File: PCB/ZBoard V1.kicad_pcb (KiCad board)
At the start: 2 copper layers, 143 parts, among them SW1 SW_Push, SW10 SW_Push, SW11 SW_Push, SW12 SW_Push, SW13 SW_Push, SW14 SW_Push, SW15 SW_Push, SW16 SW_Push, SW17 SW_Push, SW18 SW_Push, SW19 SW_Push, SW2 SW_Push, SW20 SW_Push, SW21 SW_Push, SW22 SW_Push, SW23 SW_Push, SW24 SW_Push, SW25 SW_Push, SW26 SW_Push, SW27 SW_Push, SW28 SW_Push, SW29 SW_Push, SW3 SW_Push, SW30 SW_Push, SW31 SW_Push, SW32 SW_Push, SW33 SW_Push, SW34 SW_Push, SW35 SW_Push, SW36 SW_Push, SW37 SW_Push, SW38 SW_Push, SW39 SW_Push, SW4 SW_Push, SW40 SW_Push, SW41 SW_Push, SW42 SW_Push, SW43 SW_Push, SW44 SW_Push, SW45 SW_Push, SW46 SW_Push, SW47 SW_Push, SW48 SW_Push, SW49 SW_Push, SW5 SW_Push, SW50 SW_Push, SW51 SW_Push, SW52 SW_Push, SW53 SW_Push, SW54 SW_Push, SW55 SW_Push, SW56 SW_Push, SW57 SW_Push, SW58 SW_Push, SW59 SW_Push, SW6 SW_Push, SW60 SW_Push, SW7 SW_Push, SW8 SW_Push, SW9 SW_Push, U1 XIAO-nRF52840-SMD, U2 XIAO-nRF52840-SMD

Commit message: Finish PCB routing
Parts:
- removed 2M1, 2M2, 806k1, 806k2: R, Diode_SMD:D_SOD-123
- removed BO1, BO2, BO3: break off, Mousebites:mouse-bite-5mm-slot
- removed H1, H10, H2, H3, H4, H5, H6, H7, H8, H9: MountingHole, Mousebites:mouse-bite-5mm-slot
- removed TP3, TP4: GND, TestPoint:TestPoint_Pad_D2.0mm
- added D61: D, Diode_SMD:D_SOD-123, F.Cu at (204.8, 23.8)
- added D62: D, Diode_SMD:D_SOD-123, F.Cu at (204.8, 42.9)
- added D63: D, Diode_SMD:D_SOD-123, F.Cu at (214.3, 61.9)
- added D64: D, Diode_SMD:D_SOD-123, F.Cu at (219.1, 81.0)
- added D65: D, Diode_SMD:D_SOD-123, F.Cu at (228.6, 100.0)
- added D66: D, Diode_SMD:D_SOD-123, F.Cu at (223.8, 23.8)
- added D67: D, Diode_SMD:D_SOD-123, F.Cu at (223.8, 42.9)
- added D68: D, Diode_SMD:D_SOD-123, F.Cu at (233.4, 61.9)
- added D69: D, Diode_SMD:D_SOD-123, F.Cu at (238.1, 81.0)
- added D70: D, Diode_SMD:D_SOD-123, F.Cu at (247.7, 100.0)
- added D71: D, Diode_SMD:D_SOD-123, F.Cu at (242.9, 23.8)
- added D72: D, Diode_SMD:D_SOD-123, F.Cu at (242.9, 42.9)
- added D73: D, Diode_SMD:D_SOD-123, F.Cu at (252.4, 61.9)
- added D74: D, Diode_SMD:D_SOD-123, F.Cu at (257.2, 81.0)
- added D75: D, Diode_SMD:D_SOD-123, F.Cu at (281.0, 100.0)
- added D76: D, Diode_SMD:D_SOD-123, F.Cu at (261.9, 23.8)
- added D77: D, Diode_SMD:D_SOD-123, F.Cu at (261.9, 42.9)
- added D78: D, Diode_SMD:D_SOD-123, F.Cu at (271.5, 61.9)
- added D79: D, Diode_SMD:D_SOD-123, F.Cu at (300.0, 81.0)
- added D80: D, Diode_SMD:D_SOD-123, F.Cu at (300.0, 100.0)
- added D81: D, Diode_SMD:D_SOD-123, F.Cu at (281.0, 23.8)
- added D82: D, Diode_SMD:D_SOD-123, F.Cu at (300.0, 42.9)
- added D83: D, Diode_SMD:D_SOD-123, F.Cu at (300.0, 61.9)
- added D84: D, Diode_SMD:D_SOD-123, F.Cu at (300.0, 23.8)
- added R1: 806k, MFR-25FRF52-806k:MFR-25FRF52-806k, F.Cu at (340.5, 54.8)
- added R2: 2M, MFR-25FRF52-2M:MFR-25FRF52-2M, F.Cu at (340.5, 69.1)
- added SW61: SW_Push, Gateron_KS33_Hotswap:Gateron-KS33-Hotswap-1U, F.Cu at (214.3, 23.8)
- added SW62: SW_Push, Gateron_KS33_Hotswap:Gateron-KS33-Hotswap-1U, F.Cu at (214.3, 42.9)
- added SW63: SW_Push, Gateron_KS33_Hotswap:Gateron-KS33-Hotswap-1U, F.Cu at (223.8, 61.9)
- added SW64: SW_Push, Gateron_KS33_Hotswap:Gateron-KS33-Hotswap-1U, F.Cu at (228.6, 81.0)
- added SW65: SW_Push, Gateron_KS33_Hotswap:Gateron-KS33-Hotswap-1U, F.Cu at (238.1, 100.0)
- added SW66: SW_Push, Gateron_KS33_Hotswap:Gateron-KS33-Hotswap-1U, F.Cu at (233.4, 23.8)
- added SW67: SW_Push, Gateron_KS33_Hotswap:Gateron-KS33-Hotswap-1U, F.Cu at (233.4, 42.9)
- added SW68: SW_Push, Gateron_KS33_Hotswap:Gateron-KS33-Hotswap-1U, F.Cu at (242.9, 61.9)
- added SW69: SW_Push, Gateron_KS33_Hotswap:Gateron-KS33-Hotswap-1U, F.Cu at (247.7, 81.0)
- added SW70: SW_Push, Gateron_KS33_Hotswap:Gateron-KS33-Hotswap-1.75U, F.Cu at (264.3, 100.0)
- added SW71: SW_Push, Gateron_KS33_Hotswap:Gateron-KS33-Hotswap-1U, F.Cu at (252.4, 23.8)
- added SW72: SW_Push, Gateron_KS33_Hotswap:Gateron-KS33-Hotswap-1U, F.Cu at (252.4, 42.9)
- added SW73: SW_Push, Gateron_KS33_Hotswap:Gateron-KS33-Hotswap-1U, F.Cu at (261.9, 61.9)
- added SW74: SW_Push, Gateron_KS33_Hotswap:Gateron-KS33-Hotswap-2.25U, F.Cu at (278.6, 81.0)
- added SW75: SW_Push, Gateron_KS33_Hotswap:Gateron-KS33-Hotswap-1U, F.Cu at (290.5, 100.0)
- added SW76: SW_Push, Gateron_KS33_Hotswap:Gateron-KS33-Hotswap-1U, F.Cu at (271.5, 23.8)
- added SW77: SW_Push, Gateron_KS33_Hotswap:Gateron-KS33-Hotswap-2U, F.Cu at (281.0, 42.9)
- added SW78: SW_Push, Gateron_KS33_Hotswap:Gateron-KS33-Hotswap-1.5U, F.Cu at (285.8, 61.9)
- added SW79: SW_Push, Gateron_KS33_Hotswap:Gateron-KS33-Hotswap-1U, F.Cu at (309.6, 81.0)
- added SW80: SW_Push, Gateron_KS33_Hotswap:Gateron-KS33-Hotswap-1U, F.Cu at (309.6, 100.0)
- added SW81: SW_Push, Gateron_KS33_Hotswap:Gateron-KS33-Hotswap-1U, F.Cu at (290.5, 23.8)
- added SW82: SW_Push, Gateron_KS33_Hotswap:Gateron-KS33-Hotswap-1U, F.Cu at (309.6, 42.9)
- added SW83: SW_Push, Gateron_KS33_Hotswap:Gateron-KS33-Hotswap-1U, F.Cu at (309.6, 61.9)
- added SW84: SW_Push, Gateron_KS33_Hotswap:Gateron-KS33-Hotswap-1U, F.Cu at (309.6, 23.8)
- SW1, SW10, SW11, SW13, SW14, SW15, SW16, SW17, SW19, SW2, SW20, SW21, SW22, SW23, SW25, SW26, SW27, SW28, SW29, SW30, SW31, SW32, SW33, SW34, SW35, SW36, SW37, SW38, SW39, SW40, SW41, SW42, SW43, SW44, SW45, SW46, SW47, SW48, SW49, SW50, SW51, SW52, SW53, SW54, SW55, SW56, SW57, SW58, SW59, SW60, SW7, SW8, SW9: footprint PCM_marbastlib-xp-gateron_lp:SW_KS33_HS_KS-2P02B01-02_HS_1u -> Gateron_KS33_Hotswap:Gateron-KS33-Hotswap-1U
- SW12, SW18, SW6: footprint PCM_marbastlib-xp-gateron_lp:SW_KS33_HS_KS-2P02B01-02_HS_1u -> Gateron_KS33_Hotswap:Gateron-KS33-Hotswap-1.25U
- SW24: footprint PCM_marbastlib-xp-gateron_lp:SW_KS33_HS_KS-2P02B01-02_HS_1u -> Gateron_KS33_Hotswap:Gateron-KS33-Hotswap-6.25U
- SW3: footprint PCM_marbastlib-xp-gateron_lp:SW_KS33_HS_KS-2P02B01-02_HS_1u -> Gateron_KS33_Hotswap:Gateron-KS33-Hotswap-1.5U
- SW4: footprint PCM_marbastlib-xp-gateron_lp:SW_KS33_HS_KS-2P02B01-02_HS_1u -> Gateron_KS33_Hotswap:Gateron-KS33-Hotswap-1.75U
- SW5: footprint PCM_marbastlib-xp-gateron_lp:SW_KS33_HS_KS-2P02B01-02_HS_1u -> Gateron_KS33_Hotswap:Gateron-KS33-Hotswap-2.25U
- TP2: value BAT -> GND; footprint TestPoint:TestPoint_Pad_D2.0mm -> TestPoint:TestPoint_Pad_2.0x2.0mm
- U2: value XIAO-nRF52840-SMD -> MCP23017-E_SP; footprint Modified-XIAO:modified-XIAO-nRF52840-SMD -> MCP23017_GPIO:MCP23107_GPIO
- moved TP2 306.1 mm to (340.5, 45.2)
- moved U2 281.1 mm to (330.2, 57.8)
- moved D60 255.1 mm to (300.0, 119.1), turned to -90 degrees
- moved D54 235.8 mm to (281.0, 119.1), turned to -90 degrees
- moved D48 223.6 mm to (261.9, 119.1), turned to -90 degrees
- moved D1 208.0 mm to (14.3, 23.8), turned to -90 degrees
- moved D42 203.8 mm to (242.9, 119.1), turned to -90 degrees
- moved SW60 201.6 mm to (309.6, 119.1)
- moved D7 200.2 mm to (33.3, 23.8), turned to -90 degrees
- moved D13 194.5 mm to (52.4, 23.8), turned to -90 degrees
- moved SW54 191.7 mm to (290.5, 119.1)
- moved TP1 190.4 mm to (340.5, 40.5)
- moved D3 188.6 mm to (14.3, 61.9), turned to -90 degrees
- moved D36 184.4 mm to (223.8, 119.1), turned to -90 degrees
- moved SW48 182.6 mm to (271.5, 119.1)
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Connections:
- net /left/VBAT renamed /VBAT
- D1 pad 1: /left/ROW0 -> /ROW1
- D10 pad 1: /right/ROW0 -> /ROW4
- D11 pad 1: /left/ROW0 -> /ROW5
- D12 pad 1: /right/ROW0 -> /ROW6
- D13 pad 1: /left/ROW1 -> /ROW1
- D14 pad 1: /right/ROW1 -> /ROW2
- D15 pad 1: /left/ROW1 -> /ROW3
- D16 pad 1: /right/ROW1 -> /ROW4
- D17 pad 1: /left/ROW1 -> /ROW5
- D18 pad 1: /right/ROW1 -> /ROW6
- D19 pad 1: /left/ROW1 -> /ROW1
- D2 pad 1: /right/ROW0 -> /ROW2
- D20 pad 1: /right/ROW1 -> /ROW2
- D21 pad 1: /left/ROW1 -> /ROW3
- D22 pad 1: /right/ROW1 -> /ROW4
- D23 pad 1: /left/ROW1 -> /ROW5
- D24 pad 1: /right/ROW1 -> /ROW6
- D25 pad 1: /left/ROW2 -> /ROW1
- D26 pad 1: /right/ROW2 -> /ROW2
- D27 pad 1: /left/ROW2 -> /ROW3
- D28 pad 1: /right/ROW2 -> /ROW4
- D29 pad 1: /left/ROW2 -> /ROW5
- D3 pad 1: /left/ROW0 -> /ROW3
- D30 pad 1: /right/ROW2 -> /ROW6
- D31 pad 1: /left/ROW2 -> /ROW1
- D32 pad 1: /right/ROW2 -> /ROW2
- D33 pad 1: /left/ROW2 -> /ROW3
- D34 pad 1: /right/ROW2 -> /ROW4
- D35 pad 1: /left/ROW2 -> /ROW5
- D36 pad 1: /right/ROW2 -> /ROW6
- D37 pad 1: /left/ROW3 -> /ROW1
- D38 pad 1: /right/ROW3 -> /ROW2
- D39 pad 1: /left/ROW3 -> /ROW3
- D4 pad 1: /right/ROW0 -> /ROW4
- D40 pad 1: /right/ROW3 -> /ROW4
- D41 pad 1: /left/ROW3 -> /ROW5
- D42 pad 1: /right/ROW3 -> /ROW6
- D43 pad 1: /left/ROW3 -> /ROW1
- D44 pad 1: /right/ROW3 -> /ROW2
- D45 pad 1: /left/ROW3 -> /ROW3
- D46 pad 1: /right/ROW3 -> /ROW4
- D47 pad 1: /left/ROW3 -> /ROW5
- D48 pad 1: /right/ROW3 -> /ROW6
- D49 pad 1: /left/ROW4 -> /ROW1
- D5 pad 1: /left/ROW0 -> /ROW5
- D50 pad 1: /right/ROW4 -> /ROW2
- D51 pad 1: /left/ROW4 -> /ROW3
- D52 pad 1: /right/ROW4 -> /ROW4
- D53 pad 1: /left/ROW4 -> /ROW5
- D54 pad 1: /right/ROW4 -> /ROW6
- D55 pad 1: /left/ROW4 -> /ROW1
- D56 pad 1: /right/ROW4 -> /ROW2
- D57 pad 1: /left/ROW4 -> /ROW3
- D58 pad 1: /right/ROW4 -> /ROW4
- D59 pad 1: /left/ROW4 -> /ROW5
- D6 pad 1: /right/ROW0 -> /ROW6
- D60 pad 1: /right/ROW4 -> /ROW6
- D7 pad 1: /left/ROW0 -> /ROW1
- D8 pad 1: /right/ROW0 -> /ROW2
- D9 pad 1: /left/ROW0 -> /ROW3
- SW1 pad 1: /left/COL0 -> /COL1
- SW10 pad 1: /right/COL4 -> /COL2
- SW11 pad 1: /left/COL5 -> /COL2
- SW12 pad 1: /right/COL5 -> /COL2
- SW13 pad 1: /left/COL0 -> /COL3
- SW14 pad 1: /right/COL0 -> /COL3
- SW15 pad 1: /left/COL1 -> /COL3
- SW16 pad 1: /right/COL1 -> /COL3
- SW17 pad 1: /left/COL2 -> /COL3
- SW18 pad 1: /right/COL2 -> /COL3
- SW19 pad 1: /left/COL3 -> /COL4
- SW2 pad 1: /right/COL0 -> /COL1
- SW20 pad 1: /right/COL3 -> /COL4
- SW21 pad 1: /left/COL4 -> /COL4
- SW22 pad 1: /right/COL4 -> /COL4
- SW23 pad 1: /left/COL5 -> /COL4
- SW24 pad 1: /right/COL5 -> /COL4
- SW25 pad 1: /left/COL0 -> /COL5
- SW26 pad 1: /right/COL0 -> /COL5
- SW27 pad 1: /left/COL1 -> /COL5
- SW28 pad 1: /right/COL1 -> /COL5
- SW29 pad 1: /left/COL2 -> /COL5
- SW3 pad 1: /left/COL1 -> /COL1
- SW30 pad 1: /right/COL2 -> /COL5
- SW31 pad 1: /left/COL3 -> /COL6
- SW32 pad 1: /right/COL3 -> /COL6
- SW33 pad 1: /left/COL4 -> /COL6
- SW34 pad 1: /right/COL4 -> /COL6
- SW35 pad 1: /left/COL5 -> /COL6
- SW36 pad 1: /right/COL5 -> /COL6
- SW37 pad 1: /left/COL0 -> /COL7
- SW38 pad 1: /right/COL0 -> /COL7
- SW39 pad 1: /left/COL1 -> /COL7
- SW4 pad 1: /right/COL1 -> /COL1
- SW40 pad 1: /right/COL1 -> /COL7
- SW41 pad 1: /left/COL2 -> /COL7
- SW42 pad 1: /right/COL2 -> /COL7
- SW43 pad 1: /left/COL3 -> /COL8
- SW44 pad 1: /right/COL3 -> /COL8
- SW45 pad 1: /left/COL4 -> /COL8
- SW46 pad 1: /right/COL4 -> /COL8
- SW47 pad 1: /left/COL5 -> /COL8
- SW48 pad 1: /right/COL5 -> /COL8
- SW49 pad 1: /left/COL0 -> /COL9
- SW5 pad 1: /left/COL2 -> /COL1
- SW50 pad 1: /right/COL0 -> /COL9
- SW51 pad 1: /left/COL1 -> /COL9
- SW52 pad 1: /right/COL1 -> /COL9
- SW53 pad 1: /left/COL2 -> /COL9
- SW54 pad 1: /right/COL2 -> /COL9
- SW55 pad 1: /left/COL3 -> /COL10
- SW56 pad 1: /right/COL3 -> /COL10
- SW57 pad 1: /left/COL4 -> /COL10
- SW58 pad 1: /right/COL4 -> /COL10
- SW59 pad 1: /left/COL5 -> /COL10
- SW6 pad 1: /right/COL2 -> /COL1
- SW60 pad 1: /right/COL5 -> /COL10
- SW7 pad 1: /left/COL3 -> /COL2
- SW8 pad 1: /right/COL3 -> /COL2
- SW9 pad 1: /left/COL4 -> /COL2
- TP2 pad 1: /right/VBAT -> GND
- U1 pad 1: /left/BT_PIN -> /COL15
- U1 pad 10: /left/ROW2 -> /ROW4
- U1 pad 11: /left/ROW1 -> /ROW3
- U1 pad 14: unconnected-(U1-5V-Pad14) -> +5V
- U1 pad 2: /left/COL1 -> /COL16
- U1 pad 20: /left/COL0 -> unconnected-(U1-PA30_SWCLK-Pad20)
- U1 pad 3: /left/COL2 -> /ROW6
- U1 pad 4: /left/COL3 -> /BT_PIN
- U1 pad 5: /left/COL4 -> /SDA
- U1 pad 6: /left/COL5 -> /ROW1
- U1 pad 7: /left/ROW0 -> /ROW2
- U1 pad 8: /left/ROW4 -> /ROW5
- U1 pad 9: /left/ROW3 -> /SCK
- U2 pad 1: /right/BT_PIN -> /COL8
- U2 pad 10: /right/ROW2 -> GND
- U2 pad 11: /right/ROW1 -> unconnected-(U2-NC-Pad11)
- U2 pad 12: unconnected-(U2-3V3-Pad12) -> /SCK
- U2 pad 13: GND -> /SDA
- U2 pad 15: /right/VBAT -> GND
- U2 pad 17: unconnected-(U2-NFC1-Pad17) -> GND
- U2 pad 18: unconnected-(U2-NFC2-Pad18) -> +5V
- U2 pad 2: /right/COL1 -> /COL9
- U2 pad 20: /right/COL0 -> unconnected-(U2-INTA-Pad20)
- U2 pad 21: unconnected-(U2-RESET-Pad21) -> /COL1
- U2 pad 22: unconnected-(U2-GND-Pad22) -> /COL2
- U2 pad 3: /right/COL2 -> /COL10
- U2 pad 4: /right/COL3 -> /COL11
- U2 pad 5: /right/COL4 -> /COL12
- U2 pad 6: /right/COL5 -> /COL13
- U2 pad 7: /right/ROW0 -> /COL14
- U2 pad 8: /right/ROW4 -> unconnected-(U2-GPB7-Pad8)
- U2 pad 9: /right/ROW3 -> +5V
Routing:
- net /COL1: track 0.00 -> 465.4 mm
- net /COL2: track 0.00 -> 450.6 mm
- net /COL3: track 0.00 -> 422.6 mm
- net /ROW6: track 0.00 -> 410.9 mm, vias 0 -> 13
- net /ROW5: track 0.00 -> 409.7 mm, vias 0 -> 15
- net /ROW4: track 0.00 -> 386.1 mm, vias 0 -> 17
- net /COL4: track 0.00 -> 377.3 mm, vias 0 -> 4
- net /ROW3: track 0.00 -> 366.3 mm, vias 0 -> 19
- net /COL5: track 0.00 -> 361.8 mm, vias 0 -> 2
- net /COL6: track 0.00 -> 345.0 mm, vias 0 -> 2
- net /COL7: track 0.00 -> 328.5 mm, vias 0 -> 4
- net /ROW1: track 0.00 -> 327.9 mm, vias 0 -> 17
- net /ROW2: track 0.00 -> 326.2 mm, vias 0 -> 16
- net /COL8: track 0.00 -> 311.8 mm, vias 0 -> 4
- net /COL9: track 0.00 -> 296.2 mm, vias 0 -> 3
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
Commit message: Reroute with switches on correct side
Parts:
- D1, D10, D11, D12, D13, D14, D15, D16, D17, D18, D19, D2, D20, D21, D22, D23, D24, D25, D26, D27, D28, D29, D3, D30, D31, D32, D33, D34, D35, D36, D37, D38, D39, D4, D40, D41, D42, D43, D44, D45, D46, D47, D48, D49, D5, D50, D51, D52, D53, D54, D55, D56, D57, D58, D59, D6, D60, D61, D62, D63, D64, D65, D66, D67, D68, D69, D7, D70, D71, D72, D73, D74, D75, D76, D77, D78, D79, D8, D80, D81, D82, D83, D84, D9, SW1, SW10, SW11, SW12, SW13, SW14, SW15, SW16, SW17, SW18, SW19, SW2, SW20, SW21, SW22, SW23, SW24, SW25, SW26, SW27, SW28, SW29, SW3, SW30, SW31, SW32, SW33, SW34, SW35, SW36, SW37, SW38, SW39, SW4, SW40, SW41, SW42, SW43, SW44, SW45, SW46, SW47, SW48, SW49, SW5, SW50, SW51, SW52, SW53, SW54, SW55, SW56, SW57, SW58, SW59, SW6, SW60, SW61, SW62, SW63, SW64, SW65, SW66, SW67, SW68, SW69, SW7, SW70, SW71, SW72, SW73, SW74, SW75, SW76, SW77, SW78, SW79, SW8, SW80, SW81, SW82, SW83, SW84, SW9: moved to B.Cu
- moved D24 119.1 mm to (204.8, 119.1)
- moved D74 42.9 mm to (300.0, 81.0)
- moved D5 42.9 mm to (57.1, 100.0)
- moved TP1 38.9 mm to (335.0, 79.0)
- moved D77 38.1 mm to (300.0, 42.9)
- moved TP2 35.1 mm to (331.0, 79.0)
- moved D70 33.3 mm to (281.0, 100.0)
- moved D4 33.3 mm to (47.6, 81.0)
- moved D78 28.6 mm to (300.0, 61.9)
- moved D3 28.6 mm to (42.9, 61.9)
- moved D12 23.8 mm to (61.9, 119.1)
- moved D6 23.8 mm to (38.1, 119.1)
- moved D18 23.8 mm to (85.7, 119.1)
- moved D22 19.1 mm to (104.8, 81.0)
- moved D30 19.1 mm to (223.8, 119.1)
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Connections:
- TP2 pad 1: GND -> GNDBAT
- U1 pad 16: GND -> GNDBAT
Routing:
- net GNDBAT: track 0.00 -> 78.1 mm, vias 0 -> 1
- net /COL10: track 264.2 -> 328.0 mm, vias 2 -> 1
- net /ROW5: track 409.7 -> 349.0 mm
- net GND: track 133.1 -> 77.0 mm, vias 2 -> 0
- net /COL8: track 311.8 -> 365.9 mm, vias 4 -> 1
- net /COL9: track 296.2 -> 345.6 mm, vias 3 -> 1
- net /COL6: track 345.0 -> 382.7 mm, vias 2 -> 3
- net /VBAT: track 32.7 -> 69.9 mm, vias 0 -> 1
- net /ROW4: track 386.1 -> 349.6 mm, vias 17 -> 15
- net /COL5: track 361.8 -> 398.0 mm, vias 2 -> 5
- net /COL4: track 377.3 -> 411.1 mm, vias 4 -> 5
- net /COL3: track 422.6 -> 454.5 mm, vias 0 -> 5
- net /ROW3: track 366.3 -> 337.1 mm
- net /COL1: track 465.4 -> 493.9 mm, vias 0 -> 5
- net +5V: track 72.2 -> 48.3 mm, vias 1 -> 2
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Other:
- board outline added: 333 x 119 mm
- board text added: "By Jay Golding"
- board text added: "Z"
- board text added: "ZBoard-V1"

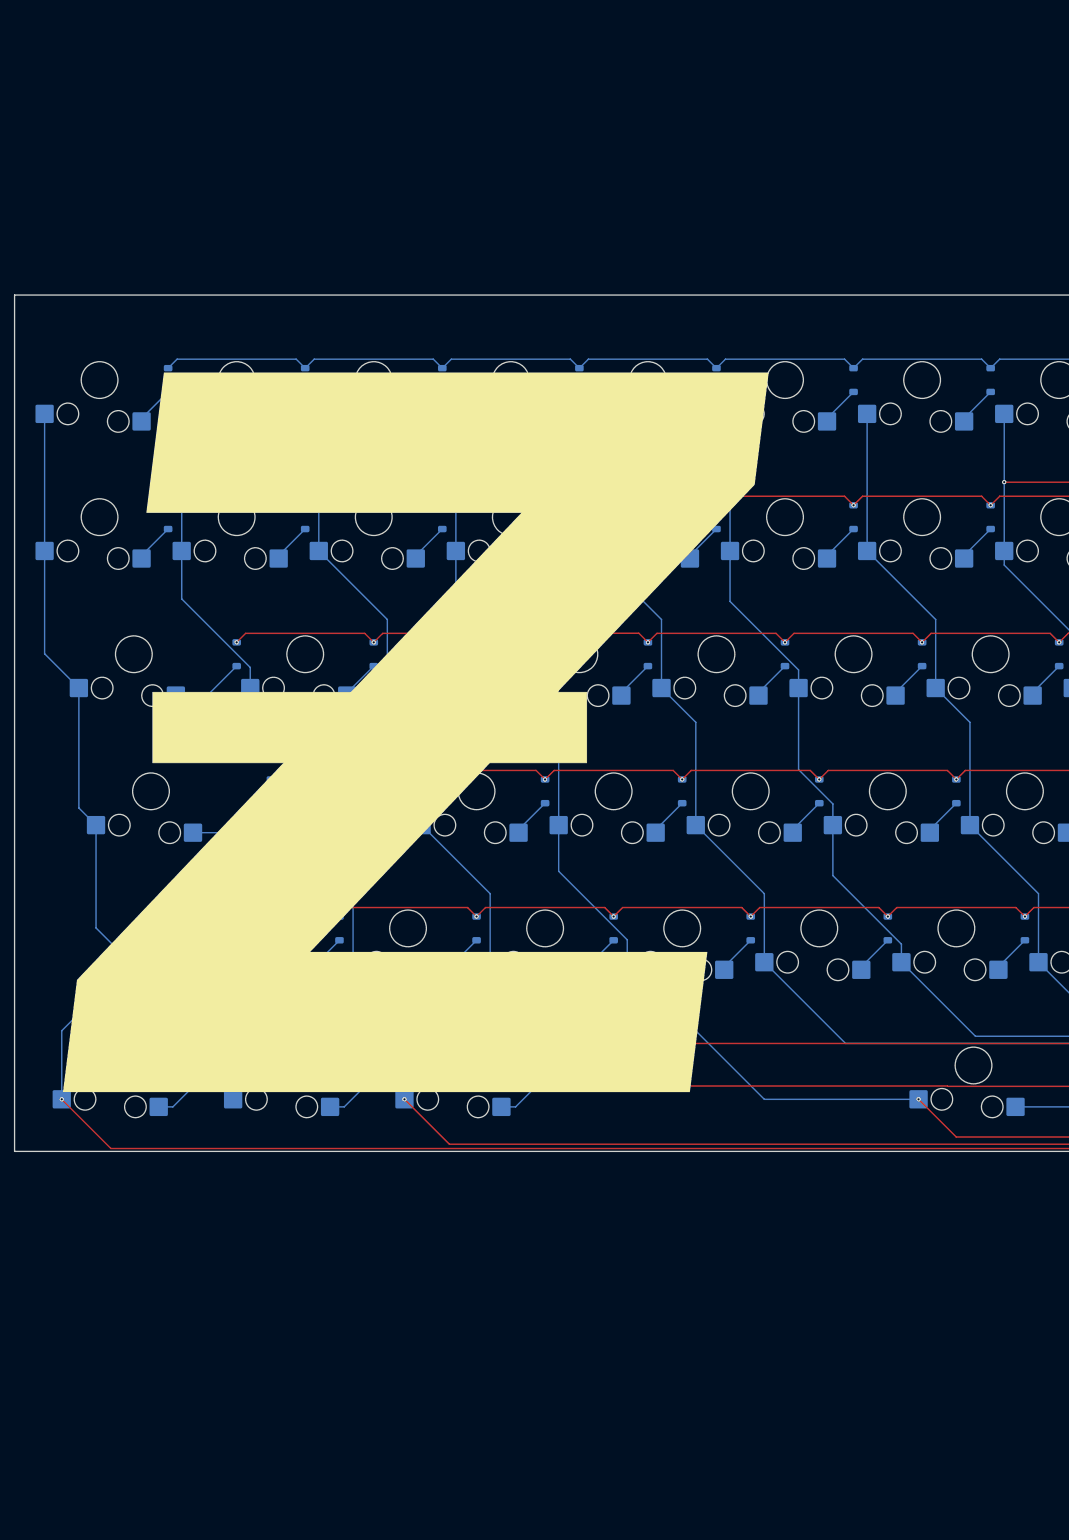
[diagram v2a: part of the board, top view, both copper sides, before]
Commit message: Update BOM with keycaps
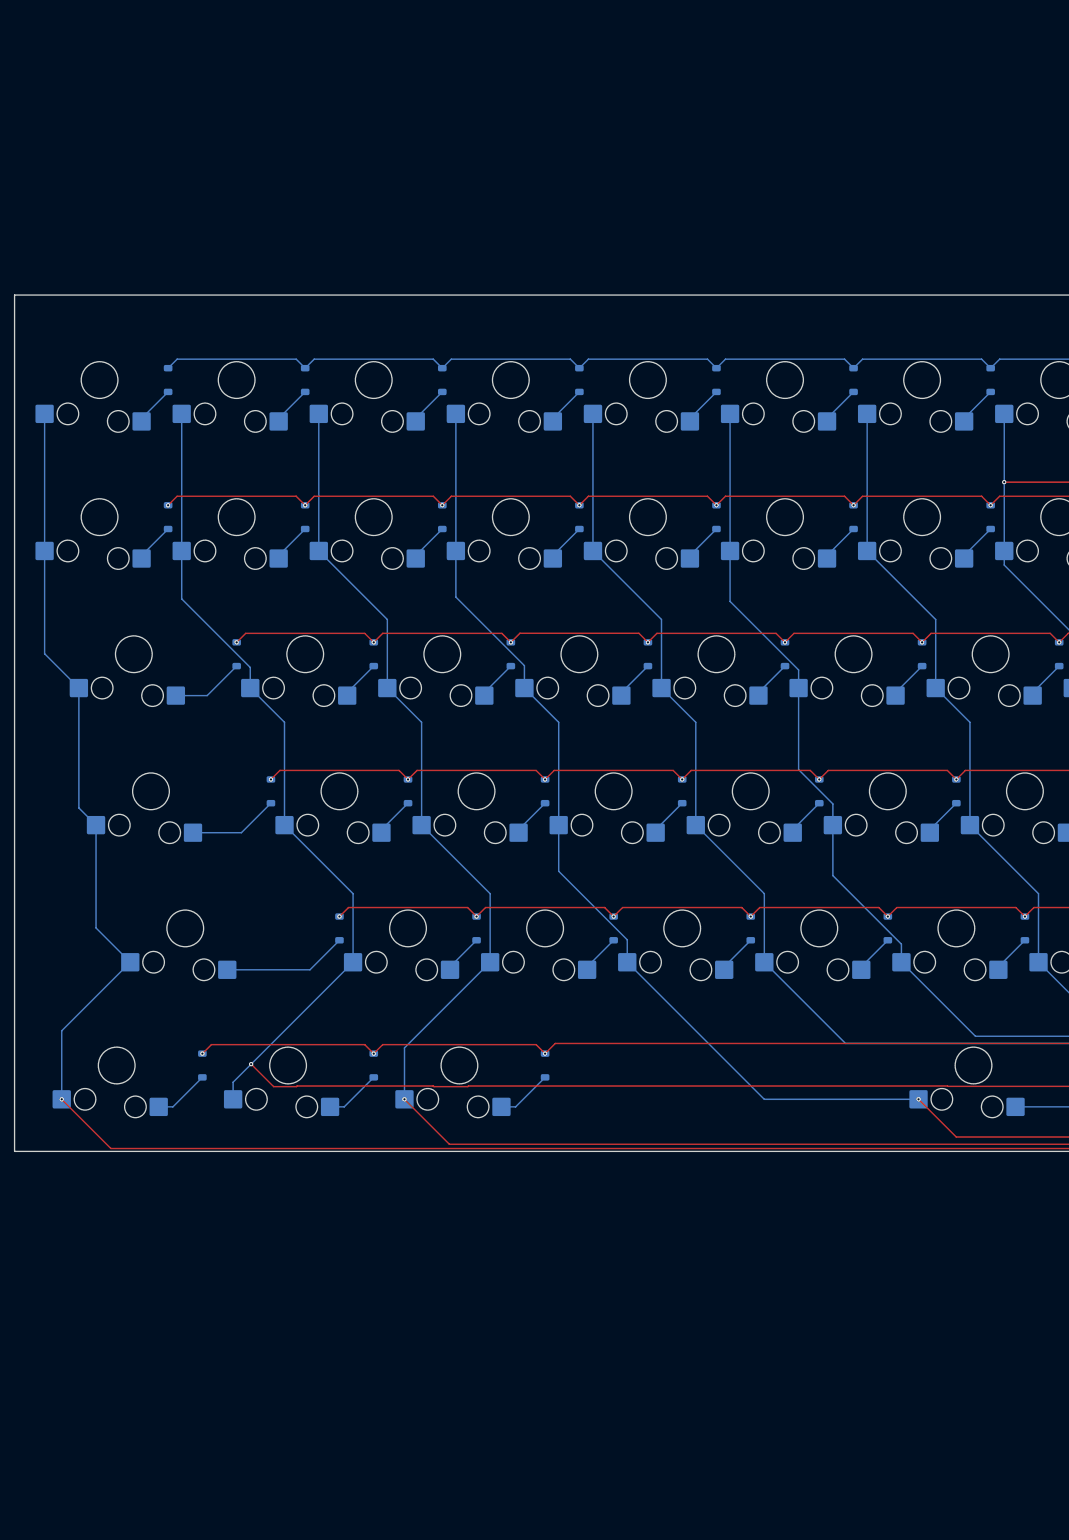
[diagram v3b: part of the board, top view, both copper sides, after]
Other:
- board text removed: "Z"
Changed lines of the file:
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@@
 		)
 		(property "Value" "D"
-			(at 0 -19.82325 -90)
+			(at 0 -19.82325 270)
 			(layer "F.Fab")
 			(effects
@@
 		)
 		(property "Value" "D"
-			(at 0 -19.82325 -90)
+			(at 0 -19.82325 270)
 			(layer "F.Fab")
 			(effects
@@
 		)
 		(property "Value" "D"
-			(at 0 -19.82325 -90)
+			(at 0 -19.82325 270)
 			(layer "F.Fab")
 			(effects
@@
 		)
 		(property "Value" "D"
-			(at 0 -19.82325 -90)
+			(at 0 -19.82325 270)
 			(layer "F.Fab")
 			(effects
@@
 		)
 		(property "Value" "D"
-			(at 0 -19.82325 -90)
+			(at 0 -19.82325 270)
 			(layer "F.Fab")
 			(effects
@@
 		)
 		(property "Value" "D"
-			(at 0 -19.82325 -90)
+			(at 0 -19.82325 270)
 			(layer "F.Fab")
 			(effects
@@
 		)
 		(fp_text user "${REFERENCE}"
-			(at 0 14.17675 -90)
+			(at 0 14.17675 270)
 			(layer "F.Fab")
 			(effects
@@
 		)
 		(property "Value" "D"
-			(at 0 -19.82325 -90)
+			(at 0 -19.82325 270)
 			(layer "F.Fab")
 			(effects
@@
 	)
 	(gr_rect
-		(start 31.2 67.2)
-		(end 91.5 77)
-		(stroke
-			(width 0.1)
-			(type solid)
-		)
-		(fill yes)
-		(layer "F.SilkS")
-	)
-	(gr_rect
 		(start 12 12)
 		(end 345 131)
@@
 		)
 	)
-	(gr_text "Z"
-		(at 12.55 135 0)
-		(layer "F.SilkS")
-		(effects
-			(font
-				(face "Source Sans Pro")
-				(size 100 100)
-				(thickness 0.2)
-				(bold yes)
-				(italic yes)
-			)
-			(justify left bottom)
-		)
-		(render_cache "Z" 0
-			(polygon
-				(pts
-					(xy 18.662177 118) (xy 80.962421 118) (xy 83.105652 107.674633) (xy 35.496615 107.674633) (xy 98.236496 32.918004)
-					(xy 99.720272 25.7739) (xy 42.085066 25.7739) (xy 39.966259 35.964933) (xy 82.775924 35.964933)
-					(xy 20.170376 110.721563)
-				)
-			)
-		)
-	)
